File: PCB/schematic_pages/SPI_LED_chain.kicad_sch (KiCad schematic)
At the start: 55 parts

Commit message: new schematics
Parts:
- C1, C10, C11, C12, C13, C14, C15, C16, C17, C18, C19, C2, C20, C21, C22, C23, C24, C25, C26, C27, C3, C4, C5, C6, C7, C8, C9: footprint (none) -> Footprints:0603_C
- C28, C29: footprint (none) -> Footprints:C_Electrolytic_4x5.4
- D1, D10, D11, D12, D13, D14, D15, D16, D17, D18, D19, D2, D20, D21, D22, D23, D24, D25, D26, D3, D4, D5, D6, D7, D8, D9: footprint (none) -> Footprints:APA102 LED
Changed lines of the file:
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@@
 			)
 		)
-		(property "Footprint" ""
+		(property "Footprint" "Footprints:C_Electrolytic_4x5.4"
 			(at 114.3 170.18 0)
 			(effects
@@
 			)
 		)
-		(property "Footprint" ""
+		(property "Footprint" "Footprints:APA102 LED"
 			(at 46.99 184.15 0)
 			(effects
@@
 			)
 		)
-		(property "Footprint" ""
+		(property "Footprint" "Footprints:APA102 LED"
 			(at 123.19 148.59 0)
 			(effects
@@
 			)
 		)
-		(property "Footprint" ""
+		(property "Footprint" "Footprints:APA102 LED"
 			(at 148.59 148.59 0)
 			(effects
@@
 			)
 		)
-		(property "Footprint" ""
+		(property "Footprint" "Footprints:APA102 LED"
 			(at 148.59 45.72 0)
 			(effects
@@
 			)
 		)
-		(property "Footprint" ""
+		(property "Footprint" "Footprints:0603_C"
 			(at 121.92 134.62 0)
 			(effects
@@
 			)
 		)
-		(property "Footprint" ""
+		(property "Footprint" "Footprints:0603_C"
 			(at 46.99 31.75 0)
 			(effects
@@
 			)
 		)
-		(property "Footprint" ""
+		(property "Footprint" "Footprints:APA102 LED"
 			(at 72.39 77.47 0)
 			(effects
@@
 			)
 		)
-		(property "Footprint" ""
+		(property "Footprint" "Footprints:APA102 LED"
 			(at 123.19 113.03 0)
 			(effects
@@
 			)
 		)
-		(property "Footprint" ""
+		(property "Footprint" "Footprints:APA102 LED"
 			(at 224.79 45.72 0)
 			(effects
@@
 			)
 		)
-		(property "Footprint" ""
+		(property "Footprint" "Footprints:0603_C"
 			(at 96.52 63.5 0)
 			(effects
@@
 			)
 		)
-		(property "Footprint" ""
+		(property "Footprint" "Footprints:0603_C"
 			(at 248.92 31.75 0)
 			(effects
@@
 			)
 		)
-		(property "Footprint" ""
+		(property "Footprint" "Footprints:0603_C"
 			(at 96.52 31.75 0)
 			(effects
@@
 			)
 		)
-		(property "Footprint" ""
+		(property "Footprint" "Footprints:APA102 LED"
 			(at 123.19 45.72 0)
 			(effects
@@
 			)
 		)
-		(property "Footprint" ""
+		(property "Footprint" "Footprints:APA102 LED"
 			(at 199.39 148.59 0)
 			(effects
@@
 			)
 		)
-		(property "Footprint" ""
+		(property "Footprint" "Footprints:0603_C"
 			(at 223.52 31.75 0)
 			(effects
@@
 			)
 		)
-		(property "Footprint" ""
+		(property "Footprint" "Footprints:APA102 LED"
 			(at 97.79 148.59 0)
 			(effects
@@
 			)
 		)
-		(property "Footprint" ""
+		(property "Footprint" "Footprints:0603_C"
 			(at 45.72 170.18 0)
 			(effects
@@
 			)
 		)
-		(property "Footprint" ""
+		(property "Footprint" "Footprints:APA102 LED"
 			(at 199.39 45.72 0)
 			(effects
@@
 			)
 		)
-		(property "Footprint" ""
+		(property "Footprint" "Footprints:0603_C"
 			(at 198.12 31.75 0)
 			(effects
@@
 			)
 		)
-		(property "Footprint" ""
+		(property "Footprint" "Footprints:APA102 LED"
 			(at 173.99 148.59 0)
 			(effects
@@
 			)
 		)
-		(property "Footprint" ""
+		(property "Footprint" "Footprints:APA102 LED"
 			(at 46.99 45.72 0)
 			(effects
@@
 			)
 		)
-		(property "Footprint" ""
+		(property "Footprint" "Footprints:0603_C"
 			(at 71.12 63.5 0)
 			(effects
@@
 			)
 		)
-		(property "Footprint" ""
+		(property "Footprint" "Footprints:0603_C"
 			(at 45.72 99.06 0)
 			(effects
@@
 			)
 		)
-		(property "Footprint" ""
+		(property "Footprint" "Footprints:0603_C"
 			(at 71.12 170.18 0)
 			(effects
@@
 			)
 		)
-		(property "Footprint" ""
+		(property "Footprint" "Footprints:0603_C"
 			(at 45.72 63.5 0)
 			(effects
@@
 			)
 		)
-		(property "Footprint" ""
+		(property "Footprint" "Footprints:APA102 LED"
 			(at 250.19 45.72 0)
 			(effects
@@
 			)
 		)
-		(property "Footprint" ""
+		(property "Footprint" "Footprints:0603_C"
 			(at 121.92 99.06 0)
 			(effects
@@
 			)
 		)
-		(property "Footprint" ""
+		(property "Footprint" "Footprints:APA102 LED"
 			(at 97.79 113.03 0)
 			(effects
@@
 			)
 		)
-		(property "Footprint" ""
+		(property "Footprint" "Footprints:0603_C"
 			(at 147.32 31.75 0)
 			(effects
@@
 			)
 		)
-		(property "Footprint" ""
+		(property "Footprint" "Footprints:0603_C"
 			(at 62.23 31.75 0)
 			(effects
@@
 			)
 		)
-		(property "Footprint" ""
+		(property "Footprint" "Footprints:0603_C"
 			(at 71.12 31.75 0)
 			(effects
@@
 			)
 		)
-		(property "Footprint" ""
+		(property "Footprint" "Footprints:APA102 LED"
 			(at 46.99 77.47 0)
 			(effects
@@
 			)
 		)
-		(property "Footprint" ""
+		(property "Footprint" "Footprints:APA102 LED"
 			(at 97.79 184.15 0)
 			(effects
@@
 			)
 		)
-		(property "Footprint" ""
+		(property "Footprint" "Footprints:0603_C"
 			(at 172.72 31.75 0)
 			(effects
@@
 			)
 		)
-		(property "Footprint" ""
+		(property "Footprint" "Footprints:0603_C"
 			(at 147.32 134.62 0)
 			(effects
@@
 			)
 		)
-		(property "Footprint" ""
+		(property "Footprint" "Footprints:APA102 LED"
 			(at 72.39 45.72 0)
 			(effects
@@
 			)
 		)
-		(property "Footprint" ""
+		(property "Footprint" "Footprints:0603_C"
 			(at 71.12 99.06 0)
 			(effects
@@
 			)
 		)
-		(property "Footprint" ""
+		(property "Footprint" "Footprints:0603_C"
 			(at 71.12 134.62 0)
 			(effects
@@
 			)
 		)
-		(property "Footprint" ""
+		(property "Footprint" "Footprints:APA102 LED"
 			(at 173.99 45.72 0)
 			(effects
@@
 			)
 		)
-		(property "Footprint" ""
+		(property "Footprint" "Footprints:APA102 LED"
 			(at 46.99 148.59 0)
 			(effects
@@
 			)
 		)
-		(property "Footprint" ""
+		(property "Footprint" "Footprints:C_Electrolytic_4x5.4"
 			(at 63.5 134.62 0)
 			(effects
@@
 			)
 		)
-		(property "Footprint" ""
+		(property "Footprint" "Footprints:APA102 LED"
 			(at 72.39 148.59 0)
 			(effects
@@
 			)
 		)
-		(property "Footprint" ""
+		(property "Footprint" "Footprints:0603_C"
 			(at 172.72 134.62 0)
 			(effects
@@
 			)
 		)
-		(property "Footprint" ""
+		(property "Footprint" "Footprints:0603_C"
 			(at 96.52 134.62 0)
 			(effects
@@
 			)
 		)
-		(property "Footprint" ""
+		(property "Footprint" "Footprints:APA102 LED"
 			(at 97.79 45.72 0)
 			(effects
@@
 			)
 		)
-		(property "Footprint" ""
+		(property "Footprint" "Footprints:0603_C"
 			(at 96.52 99.06 0)
 			(effects
@@
 			)
 		)
-		(property "Footprint" ""
+		(property "Footprint" "Footprints:0603_C"
 			(at 96.52 170.18 0)
 			(effects
@@
 			)
 		)
-		(property "Footprint" ""
+		(property "Footprint" "Footprints:0603_C"
 			(at 121.92 31.75 0)
 			(effects
@@
 			)
 		)
-		(property "Footprint" ""
+		(property "Footprint" "Footprints:APA102 LED"
 			(at 46.99 113.03 0)
 			(effects
@@
 			)
 		)
-		(property "Footprint" ""
+		(property "Footprint" "Footprints:0603_C"
 			(at 198.12 134.62 0)
 			(effects
@@
 			)
 		)
-		(property "Footprint" ""
+		(property "Footprint" "Footprints:APA102 LED"
 			(at 97.79 77.47 0)
 			(effects
@@
 			)
 		)
-		(property "Footprint" ""
+		(property "Footprint" "Footprints:APA102 LED"
 			(at 72.39 184.15 0)
 			(effects
@@
 			)
 		)
-		(property "Footprint" ""
+		(property "Footprint" "Footprints:APA102 LED"
 			(at 72.39 113.03 0)
 			(effects
@@
 			)
 		)
-		(property "Footprint" ""
+		(property "Footprint" "Footprints:0603_C"
 			(at 45.72 134.62 0)
 			(effects

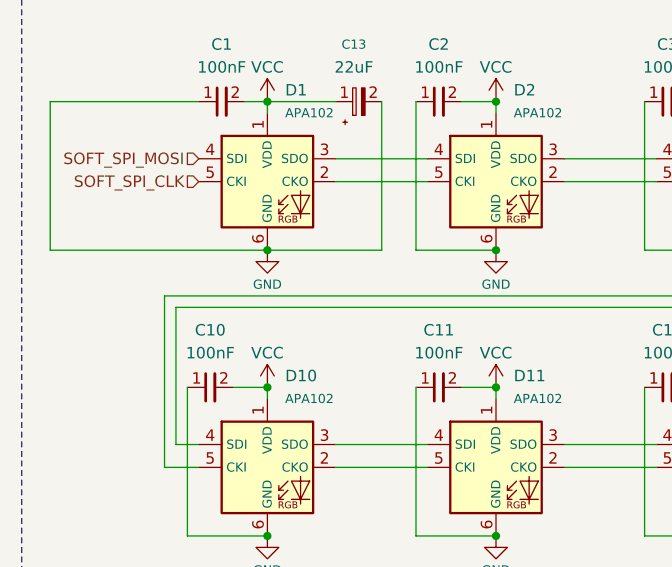
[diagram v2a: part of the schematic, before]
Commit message: ISP ports, RESET lines, MIDI DIN 5
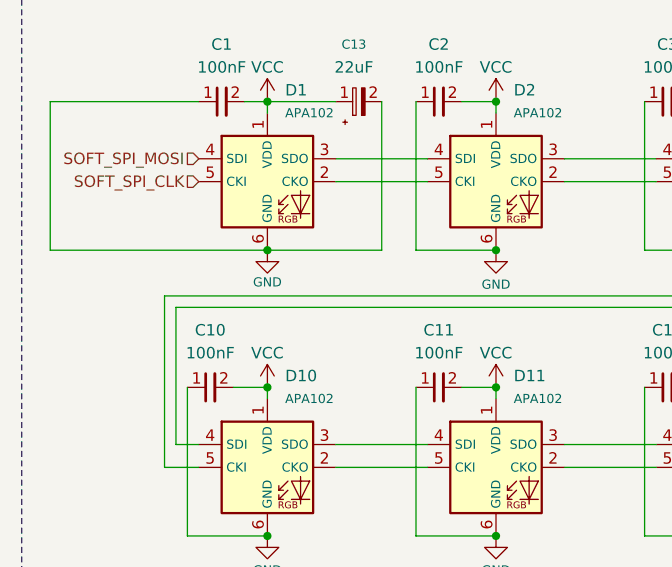
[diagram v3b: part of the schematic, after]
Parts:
- C13: footprint Footprints:0603_C -> Footprints:C_Electrolytic_4x5.4

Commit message: pcb: piano done
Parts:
- renumbered C13 to C70, C29 to C71, C28 to C72, D20 to D13, D21 to D14, D22 to D15, D23 to D16, D13 to D17, D14 to D18, D15 to D19, D16 to D20, D17 to D21, D18 to D22, D19 to D23
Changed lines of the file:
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@@
 		(dnp no)
 		(fields_autoplaced yes)
-		(property "Reference" "C29"
+		(property "Reference" "C71"
 			(at 113.7539 163.83 90)
 			(effects
@@
 			(project "MCU_328p"
 				(path "/de43e009-b04c-42c1-b131-cdc664039a0d/8c7f0436-3a68-4f5f-872d-97f6a622412c"
-					(reference "C29")
+					(reference "C71")
 					(unit 1)
 				)
@@
 		(dnp no)
 		(fields_autoplaced yes)
-		(property "Reference" "D16"
+		(property "Reference" "D20"
 			(at 130.2386 133.35 0)
 			(effects
@@
 			(project "MCU_328p"
 				(path "/de43e009-b04c-42c1-b131-cdc664039a0d/8c7f0436-3a68-4f5f-872d-97f6a622412c"
-					(reference "D16")
+					(reference "D20")
 					(unit 1)
 				)
@@
 		(dnp no)
 		(fields_autoplaced yes)
-		(property "Reference" "D17"
+		(property "Reference" "D21"
 			(at 155.6386 133.35 0)
 			(effects
@@
 			(project "MCU_328p"
 				(path "/de43e009-b04c-42c1-b131-cdc664039a0d/8c7f0436-3a68-4f5f-872d-97f6a622412c"
-					(reference "D17")
+					(reference "D21")
 					(unit 1)
 				)
@@
 		(dnp no)
 		(fields_autoplaced yes)
-		(property "Reference" "D23"
+		(property "Reference" "D16"
 			(at 130.2386 97.79 0)
 			(effects
@@
 			(project "MCU_328p"
 				(path "/de43e009-b04c-42c1-b131-cdc664039a0d/8c7f0436-3a68-4f5f-872d-97f6a622412c"
-					(reference "D23")
+					(reference "D16")
 					(unit 1)
 				)
@@
 		(dnp no)
 		(fields_autoplaced yes)
-		(property "Reference" "D19"
+		(property "Reference" "D23"
 			(at 206.4386 133.35 0)
 			(effects
@@
 			(project "MCU_328p"
 				(path "/de43e009-b04c-42c1-b131-cdc664039a0d/8c7f0436-3a68-4f5f-872d-97f6a622412c"
-					(reference "D19")
+					(reference "D23")
 					(unit 1)
 				)
@@
 		(dnp no)
 		(fields_autoplaced yes)
-		(property "Reference" "D15"
+		(property "Reference" "D19"
 			(at 104.8386 133.35 0)
 			(effects
@@
 			(project "MCU_328p"
 				(path "/de43e009-b04c-42c1-b131-cdc664039a0d/8c7f0436-3a68-4f5f-872d-97f6a622412c"
-					(reference "D15")
+					(reference "D19")
 					(unit 1)
 				)
@@
 		(dnp no)
 		(fields_autoplaced yes)
-		(property "Reference" "D18"
+		(property "Reference" "D22"
 			(at 181.0386 133.35 0)
 			(effects
@@
 			(project "MCU_328p"
 				(path "/de43e009-b04c-42c1-b131-cdc664039a0d/8c7f0436-3a68-4f5f-872d-97f6a622412c"
-					(reference "D18")
+					(reference "D22")
 					(unit 1)
 				)
@@
 		(dnp no)
 		(fields_autoplaced yes)
-		(property "Reference" "D22"
+		(property "Reference" "D15"
 			(at 104.8386 97.79 0)
 			(effects
@@
 			(project "MCU_328p"
 				(path "/de43e009-b04c-42c1-b131-cdc664039a0d/8c7f0436-3a68-4f5f-872d-97f6a622412c"
-					(reference "D22")
+					(reference "D15")
 					(unit 1)
 				)
@@
 		(dnp no)
 		(fields_autoplaced yes)
-		(property "Reference" "C13"
+		(property "Reference" "C70"
 			(at 61.6839 25.4 90)
 			(effects
@@
 			(project "MCU_328p"
 				(path "/de43e009-b04c-42c1-b131-cdc664039a0d/8c7f0436-3a68-4f5f-872d-97f6a622412c"
-					(reference "C13")
+					(reference "C70")
 					(unit 1)
 				)
@@
 		(dnp no)
 		(fields_autoplaced yes)
-		(property "Reference" "D13"
+		(property "Reference" "D17"
 			(at 54.0386 133.35 0)
 			(effects
@@
 			(project "MCU_328p"
 				(path "/de43e009-b04c-42c1-b131-cdc664039a0d/8c7f0436-3a68-4f5f-872d-97f6a622412c"
-					(reference "D13")
+					(reference "D17")
 					(unit 1)
 				)
@@
 		(dnp no)
 		(fields_autoplaced yes)
-		(property "Reference" "C28"
+		(property "Reference" "C72"
 			(at 62.9539 128.27 90)
 			(effects
@@
 			(project "MCU_328p"
 				(path "/de43e009-b04c-42c1-b131-cdc664039a0d/8c7f0436-3a68-4f5f-872d-97f6a622412c"
-					(reference "C28")
+					(reference "C72")
 					(unit 1)
 				)
@@
 		(dnp no)
 		(fields_autoplaced yes)
-		(property "Reference" "D14"
+		(property "Reference" "D18"
 			(at 79.4386 133.35 0)
 			(effects
@@
 			(project "MCU_328p"
 				(path "/de43e009-b04c-42c1-b131-cdc664039a0d/8c7f0436-3a68-4f5f-872d-97f6a622412c"
-					(reference "D14")
+					(reference "D18")
 					(unit 1)
 				)
@@
 		(on_board yes)
 		(dnp no)
-		(property "Reference" "D20"
+		(property "Reference" "D13"
 			(at 54.0386 97.79 0)
 			(effects
@@
 			(project "MCU_328p"
 				(path "/de43e009-b04c-42c1-b131-cdc664039a0d/8c7f0436-3a68-4f5f-872d-97f6a622412c"
-					(reference "D20")
+					(reference "D13")
 					(unit 1)
 				)
@@
 		(dnp no)
 		(fields_autoplaced yes)
-		(property "Reference" "D21"
+		(property "Reference" "D14"
 			(at 79.4386 97.79 0)
 			(effects
@@
 			(project "MCU_328p"
 				(path "/de43e009-b04c-42c1-b131-cdc664039a0d/8c7f0436-3a68-4f5f-872d-97f6a622412c"
-					(reference "D21")
+					(reference "D14")
 					(unit 1)
 				)
